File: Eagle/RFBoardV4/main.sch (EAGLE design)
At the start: 32 parts, among them Q1 8/16/20MHz, U1 ATMEGA328

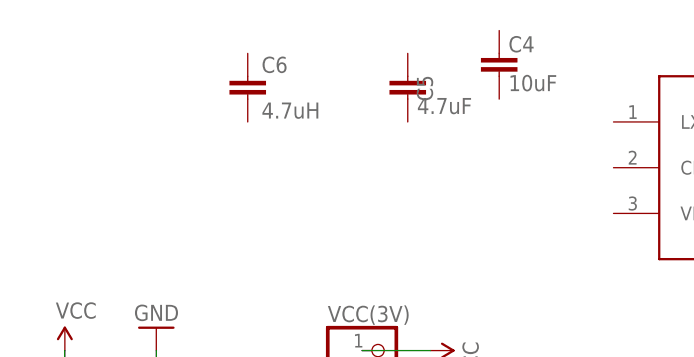
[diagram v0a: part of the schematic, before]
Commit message: Added TDK inductor
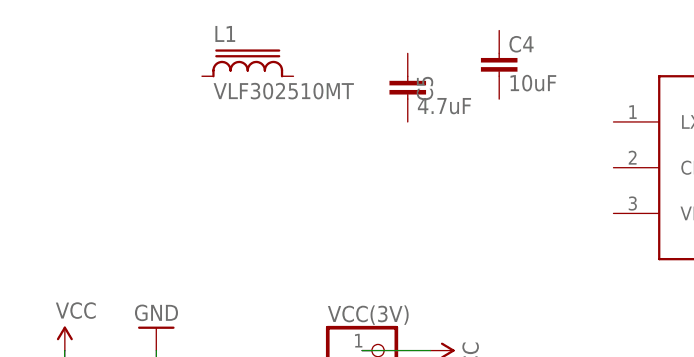
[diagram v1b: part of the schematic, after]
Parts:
- removed C6: 4.7uH, SparkFun:CAP0805
- added L1: VLF302510MT, inductor-tdk:VLF302510MT
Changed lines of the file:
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@@
 <part name="C4" library="SparkFun" deviceset="CAP" device="0603-CAP" value="10uF"/>
 <part name="C5" library="SparkFun" deviceset="CAP" device="0603-CAP" value="4.7uF"/>
-<part name="C6" library="SparkFun" deviceset="CAP" device="0805" value="4.7uH"/>
+<part name="L1" library="inductor-tdk" deviceset="VLF302510MT" device=""/>
 </parts>
 <sheets>
@@
 <attribute name="VALUE" x="54.356" y="196.469" size="1.778" layer="96"/>
 </instance>
-<instance part="C6" gate="G$1" x="35.56" y="198.12"/>
+<instance part="L1" gate="G$1" x="35.56" y="200.66"/>
 </instances>
 <busses>
